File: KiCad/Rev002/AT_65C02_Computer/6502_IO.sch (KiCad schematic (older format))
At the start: 13 parts, among them J11 LCD Connector, J2 Optional UART Port, J6 Mini-DIN-6, J8 AVR-ISP-10, J9 VIA2PA - VIA2PB, U10 ATtiny4313-PU, U11 65C22S, U12 65C22S, U5 65C51N, X2 1.8432MHz

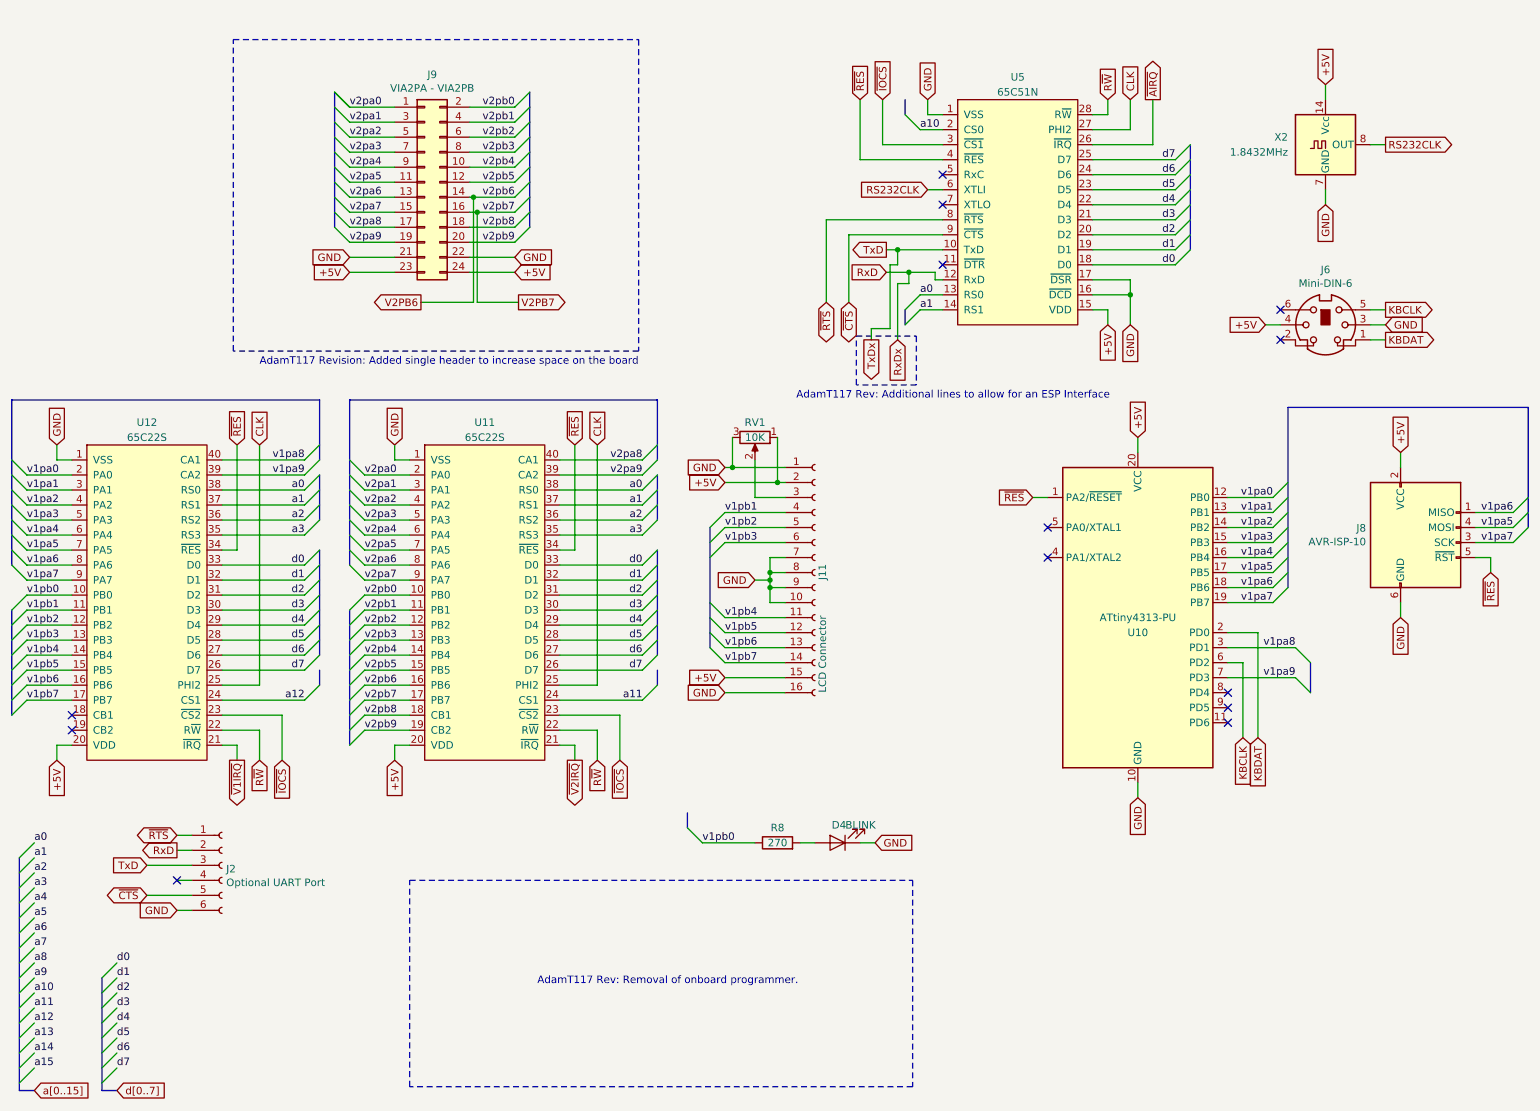
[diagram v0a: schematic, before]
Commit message: HEX Board Mods
Hex board changes. Main board Hex to Latches
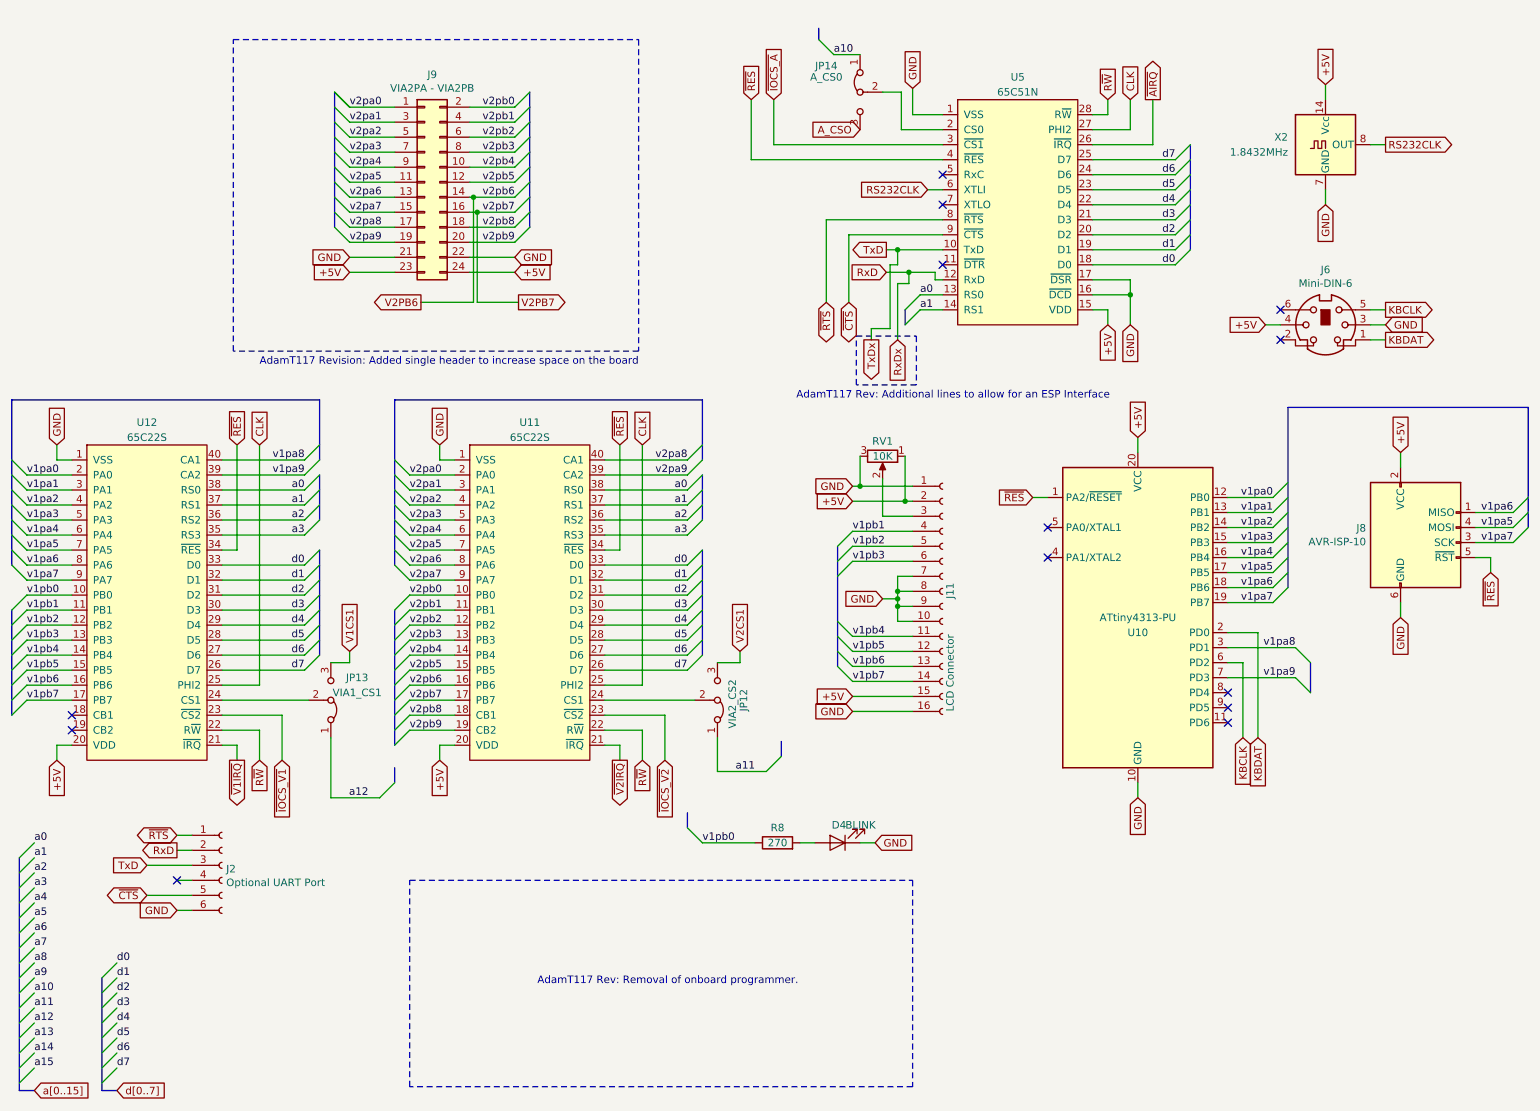
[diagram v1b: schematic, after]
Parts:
- added JP12: VIA2_CS2, Connector_PinHeader_2.54mm:PinHeader_1x03_P2.54mm_Vertical, symbol Jumper:Jumper_3_Bridged12
- added JP13: VIA1_CS1, Connector_PinHeader_2.54mm:PinHeader_1x03_P2.54mm_Vertical, symbol Jumper:Jumper_3_Bridged12
- added JP14: A_CS0, Connector_PinHeader_2.54mm:PinHeader_1x03_P2.54mm_Vertical, symbol Jumper:Jumper_3_Bridged12
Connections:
- net a10: now also JP14.1 (A); no longer U5.2 (CS0)
- net a11: now also JP12.1 (A); no longer U11.24 (CS1)
- net a12: now also JP13.1 (A); no longer U12.24 (CS1)
- removed net ~IOCS: U11.23 (~CS2), U12.23 (~CS2), U5.3 (~CS1)
- new net: JP14.2 (C), U5.2 (CS0)
- new net: JP12.2 (C), U11.24 (CS1)
- new net: JP13.2 (C), U12.24 (CS1)
- new net A_CSO: JP14.3 (B)
- new net V1CS1: JP13.3 (B)
- new net V2CS1: JP12.3 (B)
- new net ~IOCS_A: U5.3 (~CS1)
- new net ~IOCS_V1: U12.23 (~CS2)
- new net ~IOCS_V2: U11.23 (~CS2)
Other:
- moved on the sheet: J11, RV1, U11
